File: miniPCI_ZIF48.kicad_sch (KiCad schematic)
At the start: 4 parts

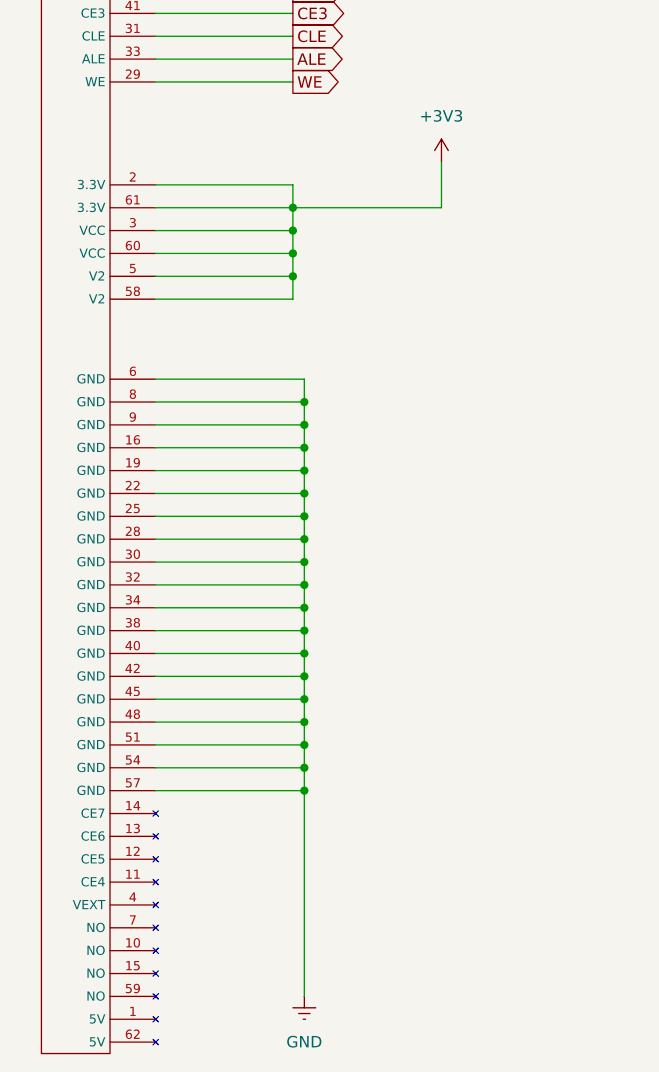
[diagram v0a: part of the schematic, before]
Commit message: Remove 3V3 & VCC from mPCI
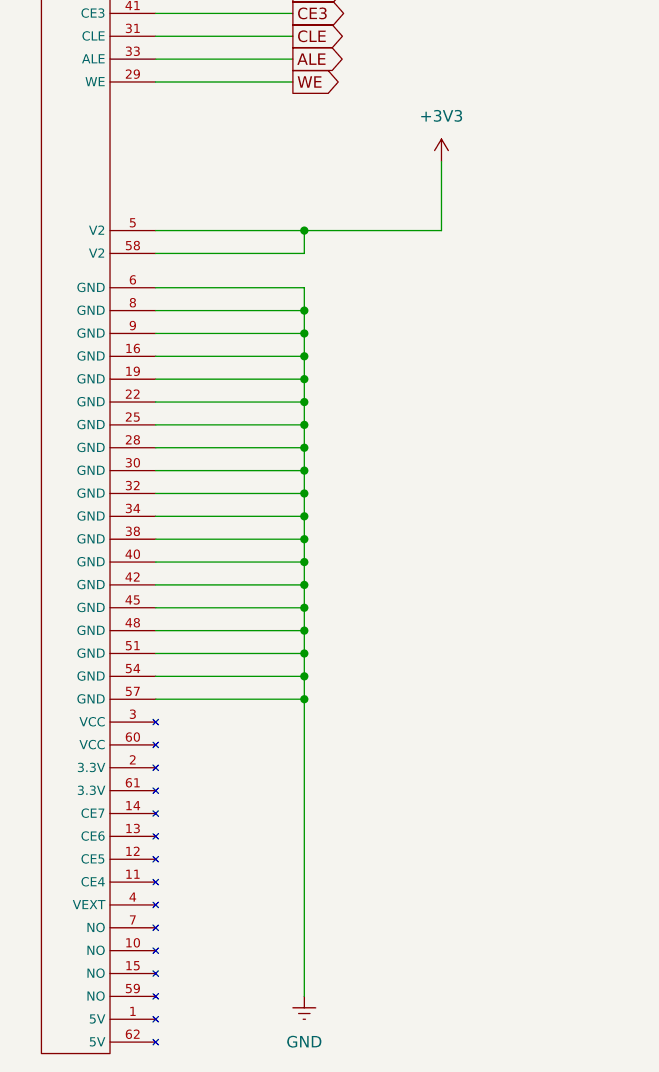
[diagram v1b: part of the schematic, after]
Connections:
- net +3V3: no longer mPCIE-62P.2 (3.3V), mPCIE-62P.3 (VCC), mPCIE-62P.60 (VCC), mPCIE-62P.61 (3.3V)

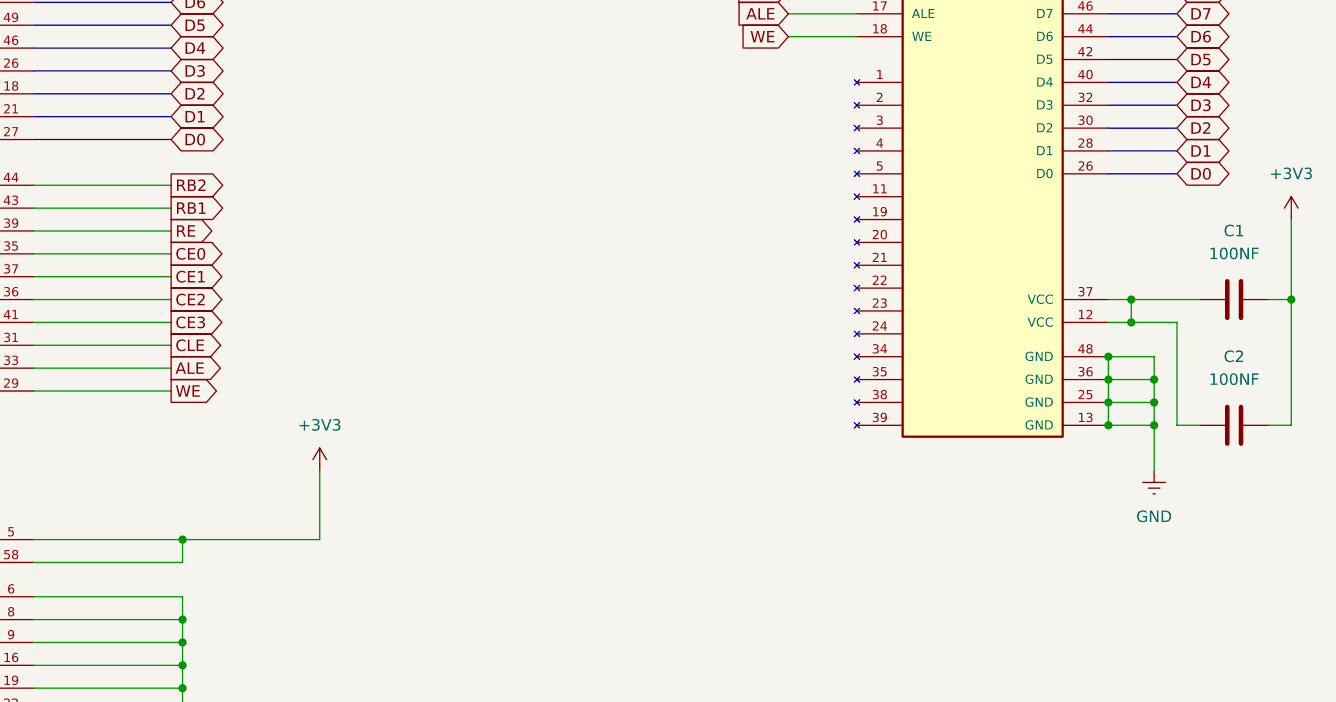
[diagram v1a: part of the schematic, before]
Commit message: Remove 2 Capacitors from ZIF/VCC & connect V2->VCC directly.
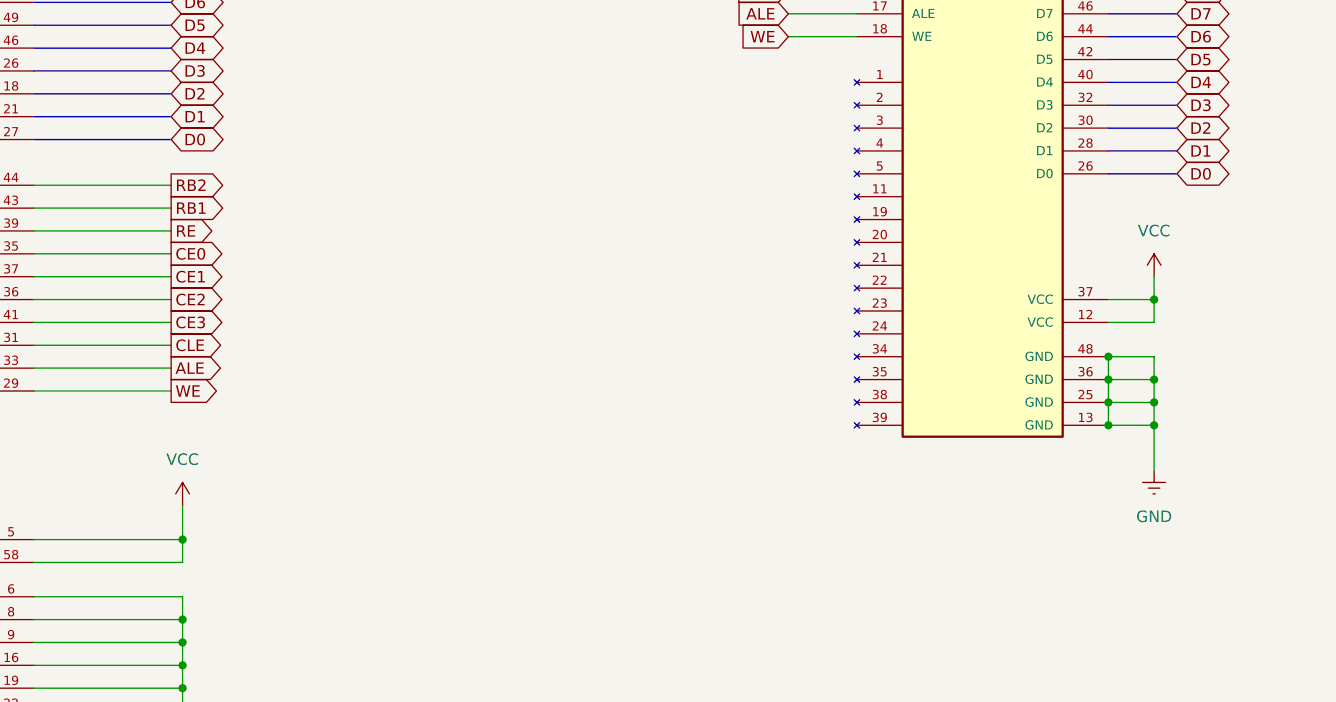
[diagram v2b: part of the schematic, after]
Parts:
- removed C1, C2: 100NF, Capacitor_SMD:C_1206_3216Metric, symbol Device:C
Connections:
- net +3V3 is gone; now on net VCC: mPCIE-62P.5 (V2), mPCIE-62P.58 (V2)
- net VCC: now reaches ZIF-48P.12 (VCC), ZIF-48P.37 (VCC)

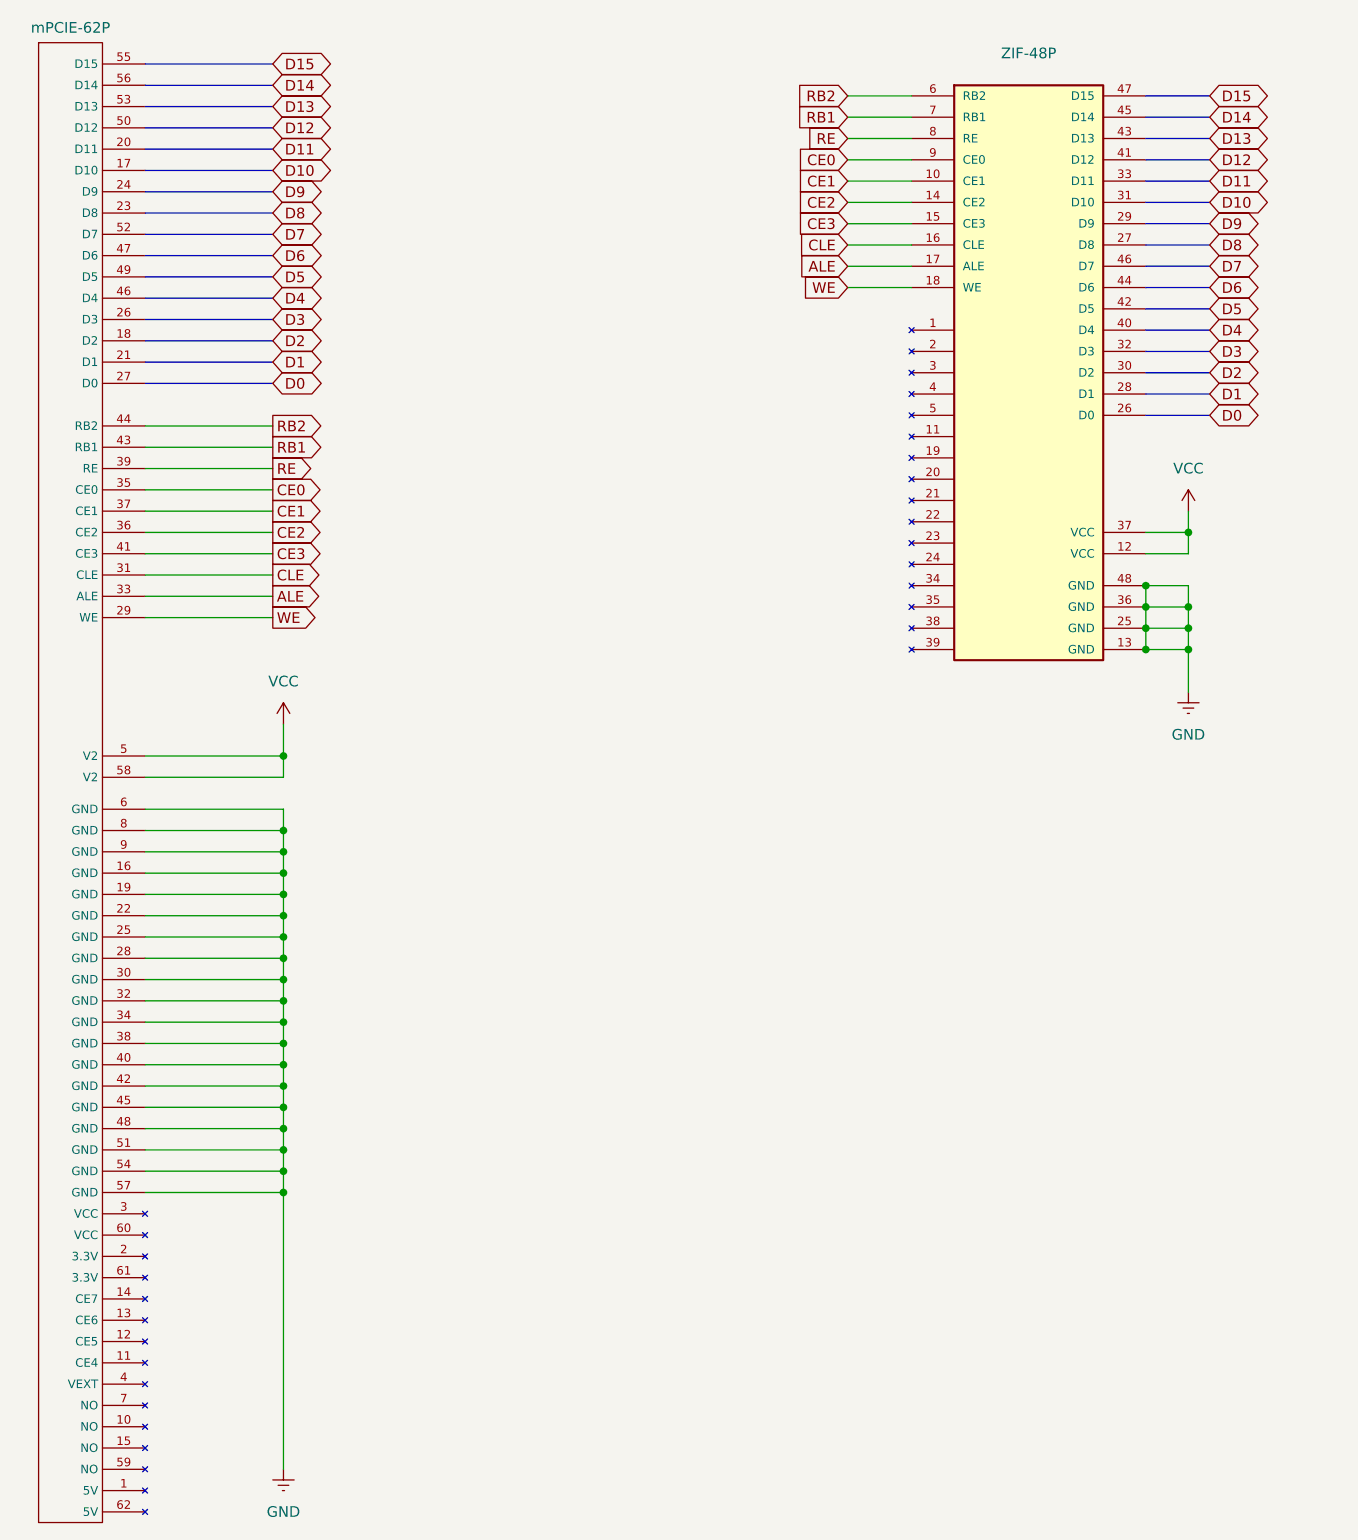
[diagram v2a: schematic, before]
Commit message: Fix decoupling capacitors to fit on each mPCI/ZIF closer & grounded.
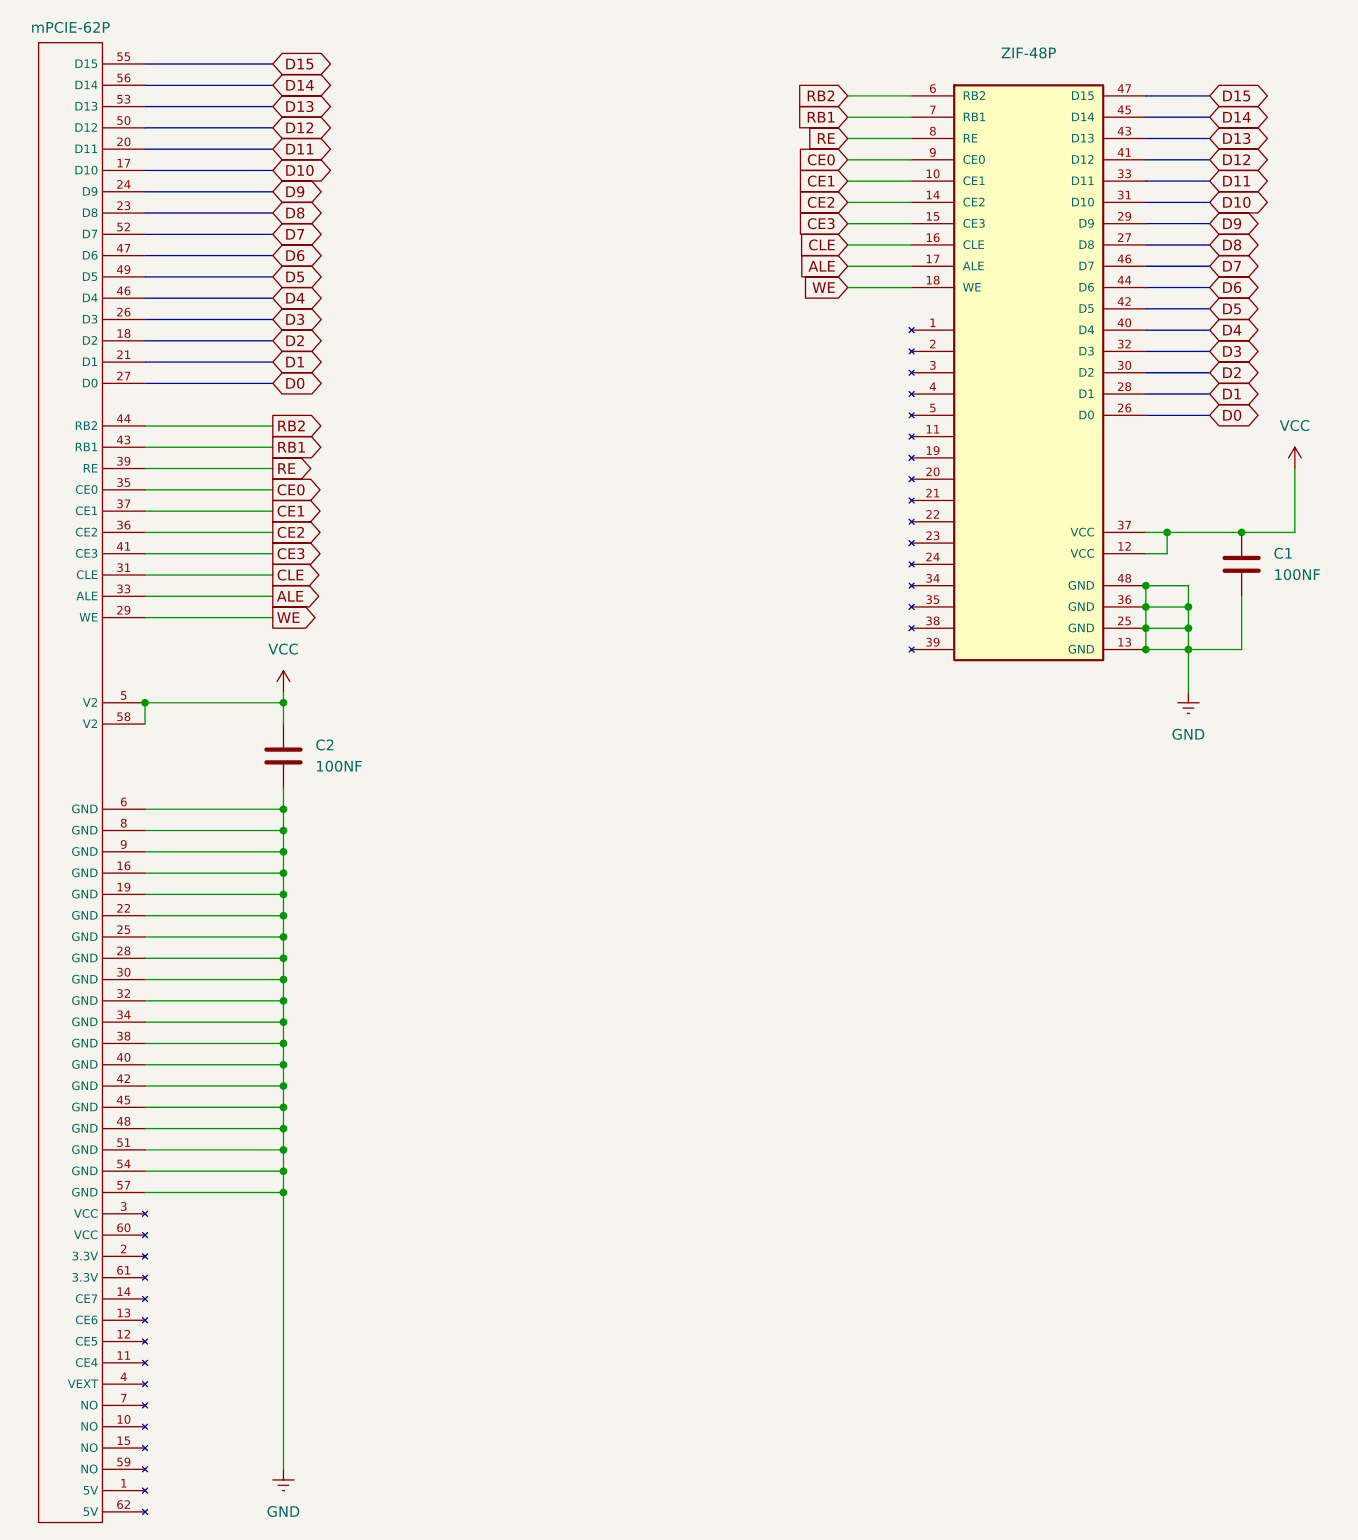
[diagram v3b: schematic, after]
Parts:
- added C1, C2: 100NF, Capacitor_SMD:C_1206_3216Metric, symbol Device:C
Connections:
- net GND: now also C1.2, C2.1
- net VCC: now also C1.1, C2.2
